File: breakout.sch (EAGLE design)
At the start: 8 parts, among them P1@1 M01PTH, P1@2 M01PTH, P2@1 M01PTH, P2@2 M01PTH, P3@1 M01PTH, P3@2 M01PTH

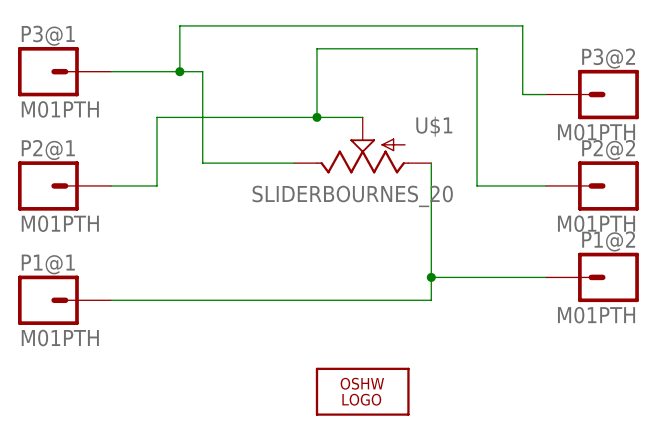
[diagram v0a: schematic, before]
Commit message: increasing font and oshw logo size
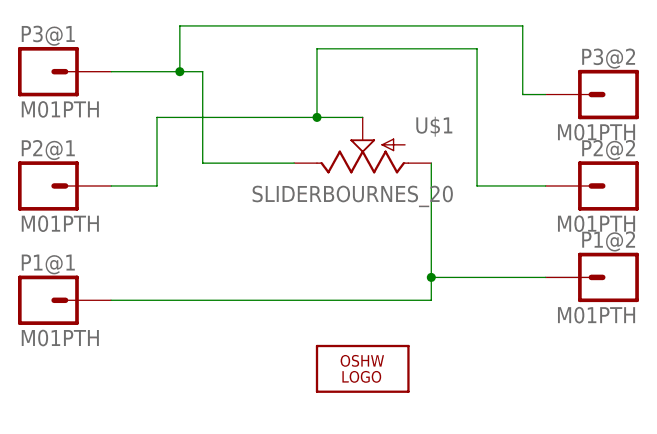
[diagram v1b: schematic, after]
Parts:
- LOGO1: value OSHW_LOGO_FILLX0070-NT -> OSHW_LOGO_FILLX0100-NT; device ohw-logo:OSHW_LOGO_FILLX0070-NT -> ohw-logo:OSHW_LOGO_FILLX0100-NT
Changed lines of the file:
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@@
 <part name="P2@2" library="SparkFun-Connectors" deviceset="M01" device="PTH"/>
 <part name="P1@2" library="SparkFun-Connectors" deviceset="M01" device="PTH"/>
-<part name="LOGO1" library="ohw-logo" deviceset="OSHW_LOGO_FILL" device="X0070-NT"/>
+<part name="LOGO1" library="ohw-logo" deviceset="OSHW_LOGO_FILL" device="X0100-NT"/>
 </parts>
 <sheets>
@@
 <instance part="P2@2" gate="G$1" x="83.82" y="45.72" rot="MR0"/>
 <instance part="P1@2" gate="G$1" x="83.82" y="35.56" rot="MR0"/>
-<instance part="LOGO1" gate="G$1" x="55.88" y="22.86"/>
+<instance part="LOGO1" gate="G$1" x="55.88" y="25.4"/>
 </instances>
 <busses>

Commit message: adding tolerance to slider tab drill holes
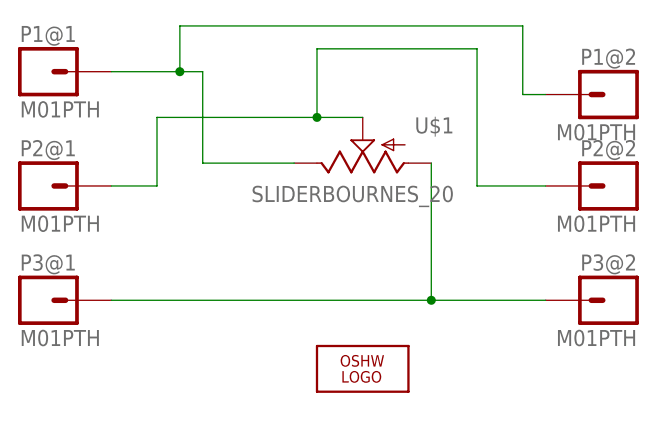
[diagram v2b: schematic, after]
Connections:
- removed net N$1: P3@1.1, P3@2.1, U$1.E
- new net N$4: P1@1.1, P1@2.1, U$1.E
- net N$3: now also P3@1.1, P3@2.1; no longer P1@1.1, P1@2.1
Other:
- moved on the sheet: P1@1, P1@2, P3@1, P3@2
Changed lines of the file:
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@@
 </plain>
 <instances>
-<instance part="P3@1" gate="G$1" x="20.32" y="58.42"/>
+<instance part="P3@1" gate="G$1" x="20.32" y="33.02"/>
 <instance part="P2@1" gate="G$1" x="20.32" y="45.72"/>
-<instance part="P1@1" gate="G$1" x="20.32" y="33.02"/>
+<instance part="P1@1" gate="G$1" x="20.32" y="58.42"/>
 <instance part="U$1" gate="G$1" x="55.88" y="48.26" rot="R90"/>
-<instance part="P3@2" gate="G$1" x="83.82" y="55.88" rot="MR0"/>
+<instance part="P3@2" gate="G$1" x="83.82" y="33.02" rot="MR0"/>
 <instance part="P2@2" gate="G$1" x="83.82" y="45.72" rot="MR0"/>
-<instance part="P1@2" gate="G$1" x="83.82" y="35.56" rot="MR0"/>
+<instance part="P1@2" gate="G$1" x="83.82" y="55.88" rot="MR0"/>
 <instance part="LOGO1" gate="G$1" x="55.88" y="25.4"/>
 </instances>
@@
 </busses>
 <nets>
-<net name="N$1" class="0">
-<segment>
-<wire x1="48.26" y1="48.26" x2="38.1" y2="48.26" width="0.1524" layer="91"/>
-<wire x1="38.1" y1="48.26" x2="38.1" y2="58.42" width="0.1524" layer="91"/>
-<pinref part="P3@1" gate="G$1" pin="1"/>
-<pinref part="U$1" gate="G$1" pin="E"/>
-<wire x1="38.1" y1="58.42" x2="35.56" y2="58.42" width="0.1524" layer="91"/>
-<pinref part="P3@2" gate="G$1" pin="1"/>
-<wire x1="35.56" y1="58.42" x2="27.94" y2="58.42" width="0.1524" layer="91"/>
-<wire x1="76.2" y1="55.88" x2="73.66" y2="55.88" width="0.1524" layer="91"/>
-<wire x1="73.66" y1="55.88" x2="73.66" y2="63.5" width="0.1524" layer="91"/>
-<wire x1="73.66" y1="63.5" x2="35.56" y2="63.5" width="0.1524" layer="91"/>
-<wire x1="35.56" y1="63.5" x2="35.56" y2="58.42" width="0.1524" layer="91"/>
-<junction x="35.56" y="58.42"/>
-</segment>
-</net>
 <net name="N$2" class="0">
 <segment>
@@
 <net name="N$3" class="0">
 <segment>
-<wire x1="63.5" y1="48.26" x2="63.5" y2="35.56" width="0.1524" layer="91"/>
-<pinref part="P1@1" gate="G$1" pin="1"/>
-<wire x1="63.5" y1="35.56" x2="63.5" y2="33.02" width="0.1524" layer="91"/>
-<wire x1="63.5" y1="33.02" x2="27.94" y2="33.02" width="0.1524" layer="91"/>
+<wire x1="63.5" y1="48.26" x2="63.5" y2="33.02" width="0.1524" layer="91"/>
 <pinref part="U$1" gate="G$1" pin="A"/>
-<pinref part="P1@2" gate="G$1" pin="1"/>
-<wire x1="76.2" y1="35.56" x2="63.5" y2="35.56" width="0.1524" layer="91"/>
-<junction x="63.5" y="35.56"/>
+<pinref part="P3@1" gate="G$1" pin="1"/>
+<wire x1="27.94" y1="33.02" x2="63.5" y2="33.02" width="0.1524" layer="91"/>
+<pinref part="P3@2" gate="G$1" pin="1"/>
+<wire x1="76.2" y1="33.02" x2="63.5" y2="33.02" width="0.1524" layer="91"/>
+<junction x="63.5" y="33.02"/>
 </segment>
 </net>
+<net name="N$4" class="0">
+<segment>
+<pinref part="U$1" gate="G$1" pin="E"/>
+<wire x1="48.26" y1="48.26" x2="38.1" y2="48.26" width="0.1524" layer="91"/>
+<wire x1="38.1" y1="48.26" x2="38.1" y2="58.42" width="0.1524" layer="91"/>
+<wire x1="38.1" y1="58.42" x2="35.56" y2="58.42" width="0.1524" layer="91"/>
+<pinref part="P1@1" gate="G$1" pin="1"/>
+<wire x1="35.56" y1="58.42" x2="27.94" y2="58.42" width="0.1524" layer="91"/>
+<wire x1="73.66" y1="55.88" x2="73.66" y2="63.5" width="0.1524" layer="91"/>
+<wire x1="73.66" y1="63.5" x2="35.56" y2="63.5" width="0.1524" layer="91"/>
+<wire x1="35.56" y1="58.42" x2="35.56" y2="63.5" width="0.1524" layer="91"/>
+<junction x="35.56" y="58.42"/>
+<pinref part="P1@2" gate="G$1" pin="1"/>
+<wire x1="73.66" y1="55.88" x2="76.2" y2="55.88" width="0.1524" layer="91"/>
+</segment>
+</net>
